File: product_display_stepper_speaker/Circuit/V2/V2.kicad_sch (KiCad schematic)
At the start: 15 parts, among them J1 Barrel_Jack_MountingPin, P1 Button, U1 L7805, U2 LD33v

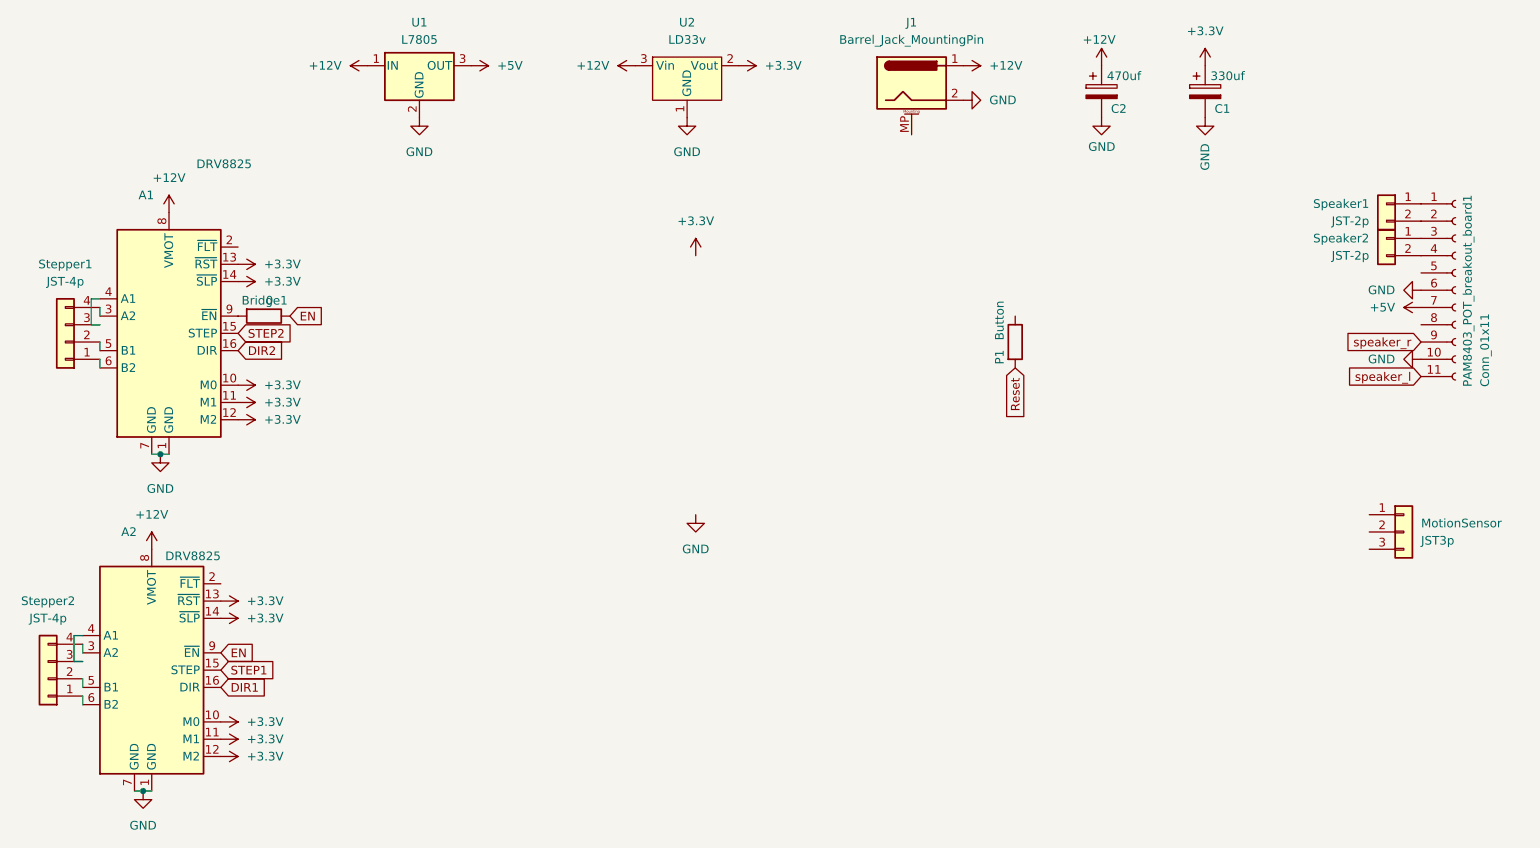
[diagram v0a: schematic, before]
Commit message: started programming hospital robot Main board
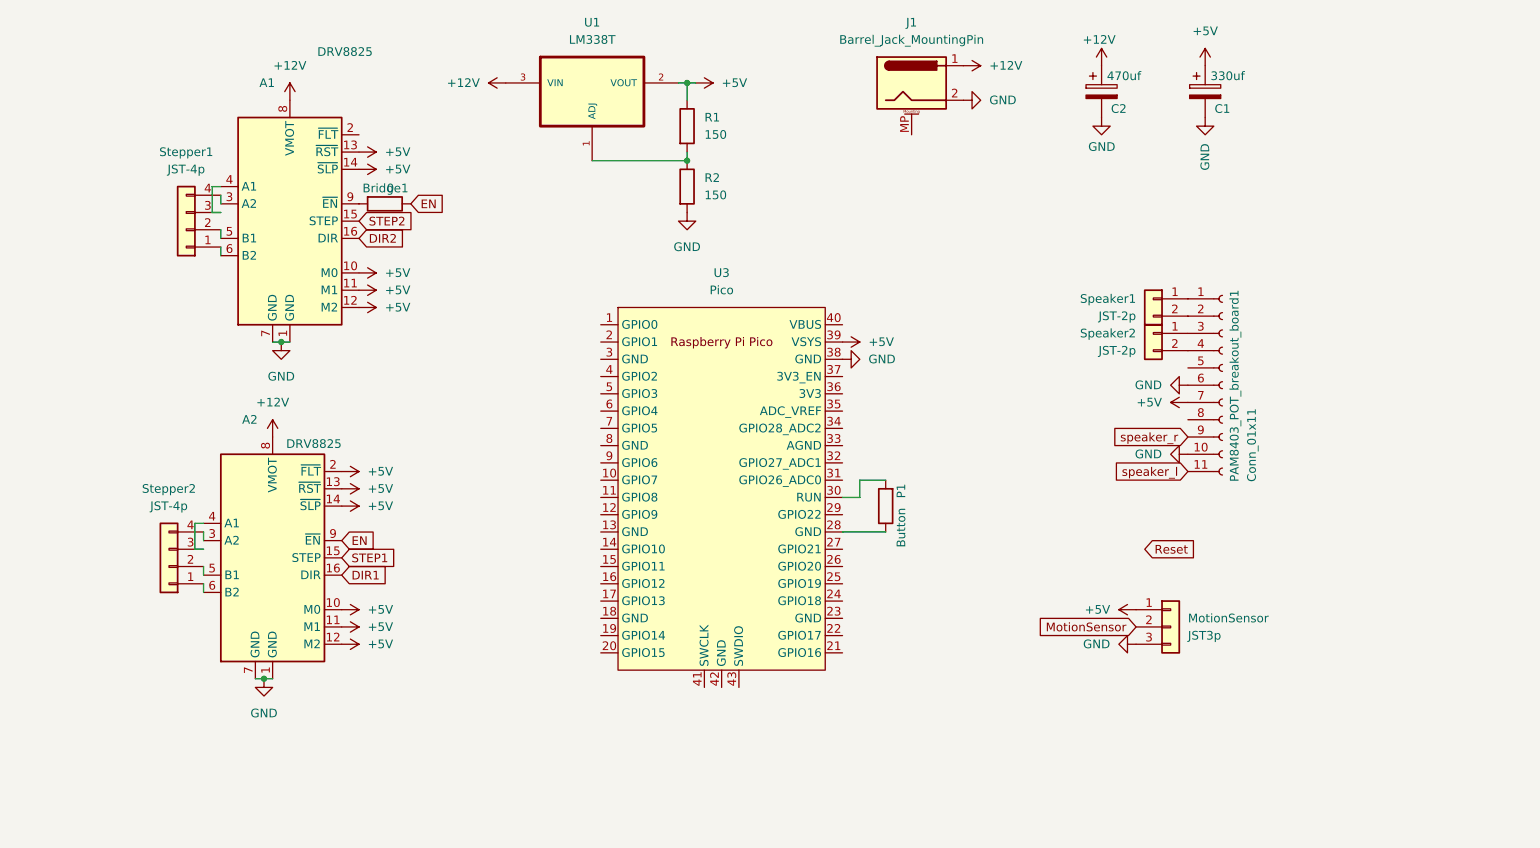
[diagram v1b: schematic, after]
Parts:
- removed U1: L7805, Package_TO_SOT_THT:TO-220-3_Vertical, symbol Regulator_Linear:L7805
- removed U2: LD33v, Package_TO_SOT_THT:TO-220-3_Vertical, symbol ld33v:LD33v
- added R1, R2: 150, Resistor_THT:R_Axial_DIN0207_L6.3mm_D2.5mm_P7.62mm_Horizontal, symbol Device:R
- added U1: LM338T, LM338T:TO254P1054X470X1955-3, symbol LM338T:LM338T
- added U3: Pico, MCU_RaspberryPi_and_Boards:RPi_Pico_SMD_TH, symbol MCU_RaspberryPi_and_Boards:Pico
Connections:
- net +3.3V is gone; now on net +5V: A1.10 (M0), A1.11 (M1), A1.12 (M2), A1.13 (~{RST}), A1.14 (~{SLP}), A2.10 (M0), A2.11 (M1), A2.12 (M2), A2.13 (~{RST}), A2.14 (~{SLP}), C1.1
- net +12V: now also U1.3 (VIN)
- net +5V: now also A2.2 (~{FLT}), MotionSensor.1 (Pin_1), R1.1, U1.2 (VOUT), U3.39 (VSYS)
- net GND: now also MotionSensor.3 (Pin_3), R2.2, U3.38 (GND)
- net Reset: no longer P1.2
- net at P1.1: now also U3.28 (GND)
- net MotionSensor: now reaches MotionSensor.2 (Pin_2)
- new net: P1.2, U3.30 (RUN)
- new net: R1.2, R2.1, U1.1 (ADJ)
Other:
- moved on the sheet: A1, A2, Bridge1, MotionSensor, P1, PAM8403_POT_breakout_board1, Speaker1, Speaker2, Stepper1, Stepper2

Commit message: finished station circuit PCB and started V2 product display stepper speaker circuit
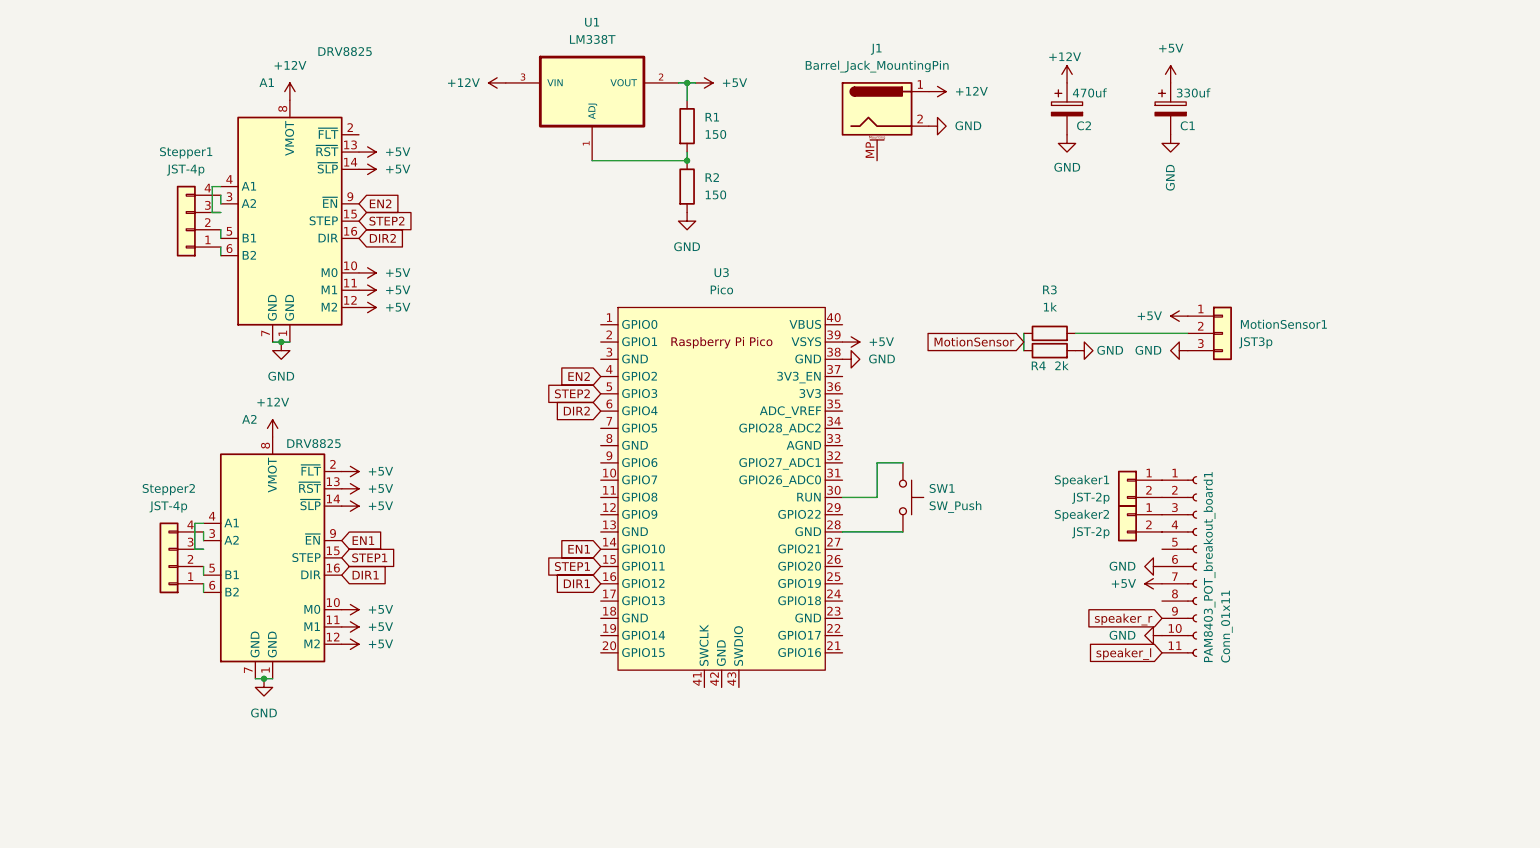
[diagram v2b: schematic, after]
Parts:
- removed Bridge1: 0, Resistor_THT:R_Axial_DIN0207_L6.3mm_D2.5mm_P7.62mm_Horizontal, symbol Device:R
- removed P1: Button, Resistor_THT:R_Axial_DIN0207_L6.3mm_D2.5mm_P5.08mm_Vertical, symbol Device:R
- added R3: 1k, Resistor_THT:R_Axial_DIN0207_L6.3mm_D2.5mm_P7.62mm_Horizontal, symbol Device:R
- added R4: 2k, Resistor_THT:R_Axial_DIN0207_L6.3mm_D2.5mm_P7.62mm_Horizontal, symbol Device:R
- added SW1: SW_Push, Button_Switch_THT:SW_PUSH_6mm, symbol Switch:SW_Push
- renumbered MotionSensor to MotionSensor1
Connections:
- net EN is gone; now on net EN1: A2.9 (~{EN})
- net DIR1: now also U3.16 (GPIO12)
- net DIR2: now also U3.6 (GPIO4)
- net GND: now also R4.2
- net MotionSensor: now also R3.1, R4.1; no longer MotionSensor1.2 (Pin_2)
- net STEP1: now also U3.15 (GPIO11)
- net STEP2: now also U3.5 (GPIO3)
- net EN1: now reaches U3.14 (GPIO10)
- net at U3.28 (GND): now also SW1.2
- net at U3.30 (RUN): now also SW1.1
- net EN2: now reaches U3.4 (GPIO2)
- net EN2: now also A1.9 (~{EN})
- new net: MotionSensor1.2 (Pin_2), R3.2
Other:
- moved on the sheet: C1, C2, J1, MotionSensor1, PAM8403_POT_breakout_board1, Speaker1, Speaker2

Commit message: finished product display stepper speaker circuit V2 PCB layout and generated gerber files and PDFs
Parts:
- added H1, H2: MountingHole, MountingHole:MountingHole_3.2mm_M3, symbol Mechanical:MountingHole
- J1: value Barrel_Jack_MountingPin -> Barrel_Jack
- R2: value 150 -> 470
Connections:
- net +5V: no longer A2.2 (~{FLT})
- net DIR1: now also U3.14 (GPIO10); no longer U3.16 (GPIO12)
- net DIR2: now also U3.4 (GPIO2); no longer U3.6 (GPIO4)
- net EN1: now also U3.16 (GPIO12); no longer U3.14 (GPIO10)
- net EN2: now also U3.6 (GPIO4); no longer U3.4 (GPIO2)
- net MotionSensor: now also U3.25 (GPIO19)
- net speaker_l: now also U3.22 (GPIO17)
- net speaker_r: now also U3.24 (GPIO18)
